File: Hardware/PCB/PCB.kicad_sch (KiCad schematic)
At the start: 0 parts

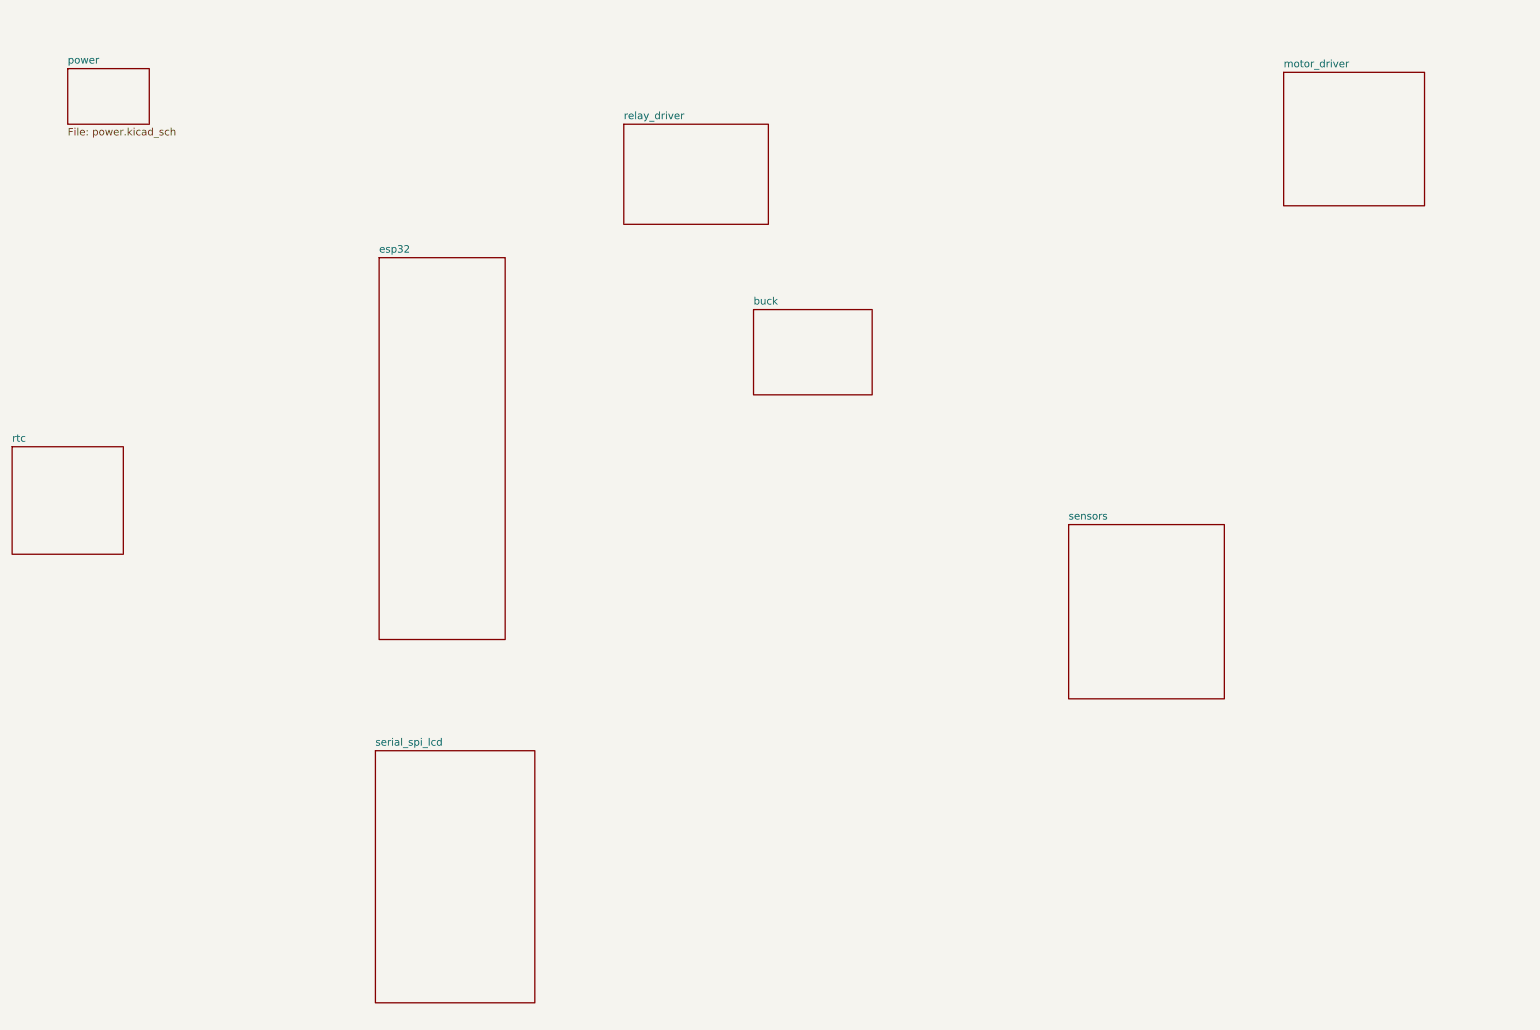
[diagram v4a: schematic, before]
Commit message: consolidated IO for LCD block, broke out hierarchial pins, need to start wiring everything up and then on to layout
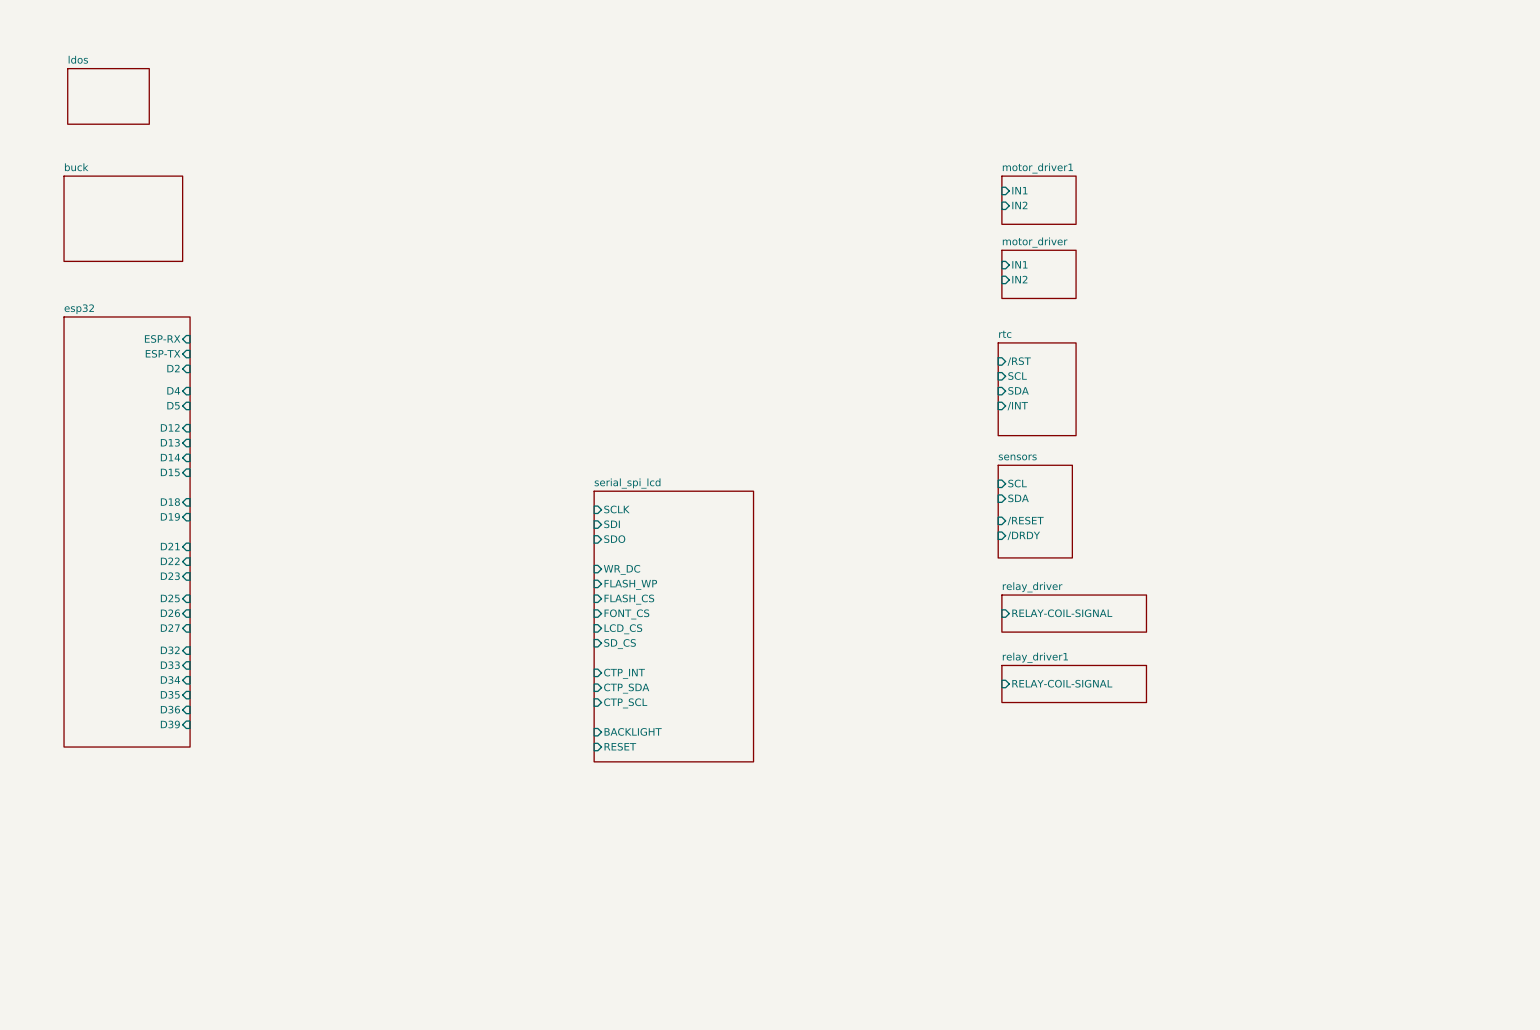
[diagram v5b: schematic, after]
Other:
- sheet power renamed ldos
- added sheet motor_driver1 (motor_driver.kicad_sch)
- added sheet relay_driver1 (relay_driver.kicad_sch)
- sheet esp32 ports: added D12, D13, D14, D15, D18, D19, D2, D21, D22, D23, D25, D26, D27, D32, D33, D34, D35, D36, D39, D4, D5, ESP-RX, ESP-TX; removed none
- sheet ldos: file power.kicad_sch -> ldos.kicad_sch
- sheet motor_driver ports: added IN1, IN2; removed none
- sheet relay_driver ports: added RELAY-COIL-SIGNAL; removed none
- sheet rtc ports: added SCL, SDA, /INT, /RST; removed none
- sheet sensors ports: added SCL, SDA, /DRDY, /RESET; removed none
- sheet serial_spi_lcd ports: added BACKLIGHT, CTP_INT, CTP_SCL, CTP_SDA, FLASH_CS, FLASH_WP, FONT_CS, LCD_CS, RESET, SCLK, SDI, SDO, SD_CS, WR_DC; removed none

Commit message: overall design is pretty much done, starting layout and routing now
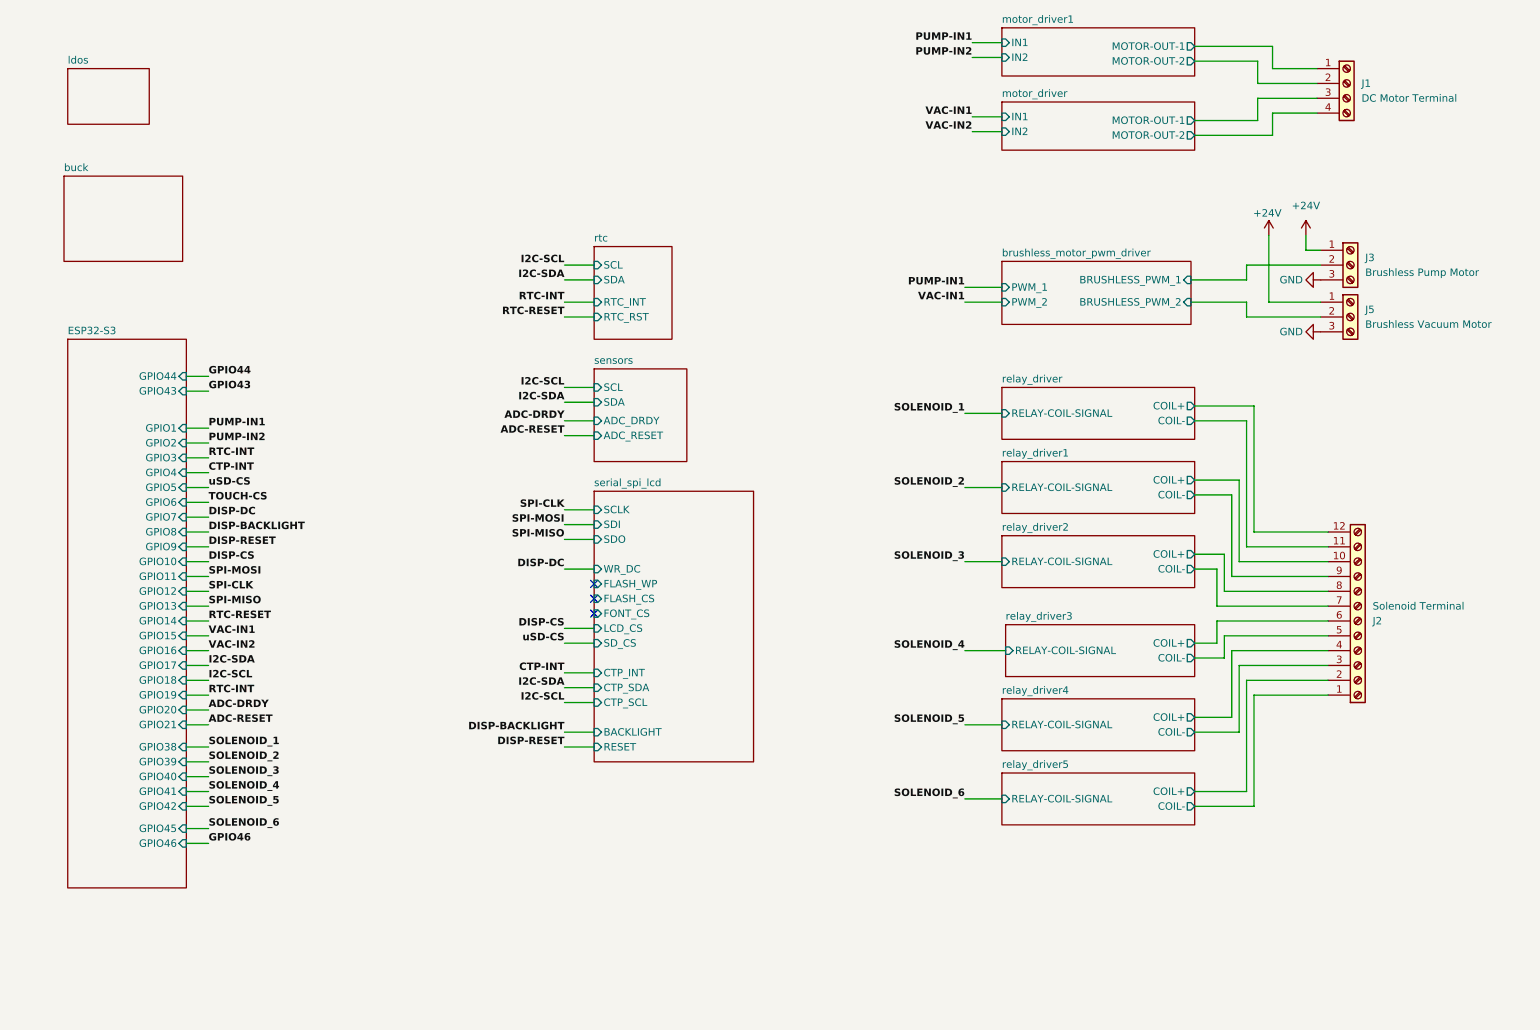
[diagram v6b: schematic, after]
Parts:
- added J1: DC Motor Terminal, Vendor_Footprints:TE_1985218, symbol Connector:Screw_Terminal_01x04
- added J2: Solenoid Terminal, Vendor_Footprints:PHX_16PIN_1985292, symbol Connector:Screw_Terminal_01x12
- added J3: Brushless Pump Motor, Vendor_Footprints:TE_1985205, symbol Connector:Screw_Terminal_01x03
- added J5: Brushless Vacuum Motor, Vendor_Footprints:TE_1985205, symbol Connector:Screw_Terminal_01x03
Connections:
- new net +24V: J3.1 (Pin_1), J5.1 (Pin_1)
- new net GND: J3.3 (Pin_3), J5.3 (Pin_3)
- new net brushless_motor_pwm_driver/BRUSHLESS_PWM_1: J3.2 (Pin_2)
- new net brushless_motor_pwm_driver/BRUSHLESS_PWM_2: J5.2 (Pin_2)
- new net motor_driver/MOTOR-OUT-1: J1.3 (Pin_3)
- new net motor_driver/MOTOR-OUT-2: J1.4 (Pin_4)
- new net motor_driver1/MOTOR-OUT-1: J1.1 (Pin_1)
- new net motor_driver1/MOTOR-OUT-2: J1.2 (Pin_2)
- new net relay_driver/COIL+: J2.12 (Pin_12)
- new net relay_driver/COIL-: J2.11 (Pin_11)
- new net relay_driver1/COIL+: J2.10 (Pin_10)
- new net relay_driver1/COIL-: J2.9 (Pin_9)
- new net relay_driver2/COIL+: J2.8 (Pin_8)
- new net relay_driver2/COIL-: J2.7 (Pin_7)
- new net relay_driver3/COIL+: J2.6 (Pin_6)
- new net relay_driver3/COIL-: J2.5 (Pin_5)
- new net relay_driver4/COIL+: J2.4 (Pin_4)
- new net relay_driver4/COIL-: J2.3 (Pin_3)
- new net relay_driver5/COIL+: J2.2 (Pin_2)
- new net relay_driver5/COIL-: J2.1 (Pin_1)
- no-connect marks 0 -> 3
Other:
- removed sheet esp32
- added sheet ESP32-S3 (esp32.kicad_sch)
- added sheet brushless_motor_pwm_driver (brushless_motor_pwm_driver.kicad_sch)
- added sheet relay_driver2 (relay_driver.kicad_sch)
- added sheet relay_driver3 (relay_driver.kicad_sch)
- added sheet relay_driver4 (relay_driver.kicad_sch)
- added sheet relay_driver5 (relay_driver.kicad_sch)
- sheet motor_driver ports: added MOTOR-OUT-1, MOTOR-OUT-2; removed none
- sheet motor_driver1 ports: added MOTOR-OUT-1, MOTOR-OUT-2; removed none
- sheet relay_driver ports: added COIL+, COIL-; removed none
- sheet relay_driver1 ports: added COIL+, COIL-; removed none
- sheet rtc ports: added RTC_INT, RTC_RST; removed /INT, /RST
- sheet sensors ports: added ADC_DRDY, ADC_RESET; removed /DRDY, /RESET

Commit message: pcb layout and routing pretty much done, checking DRC
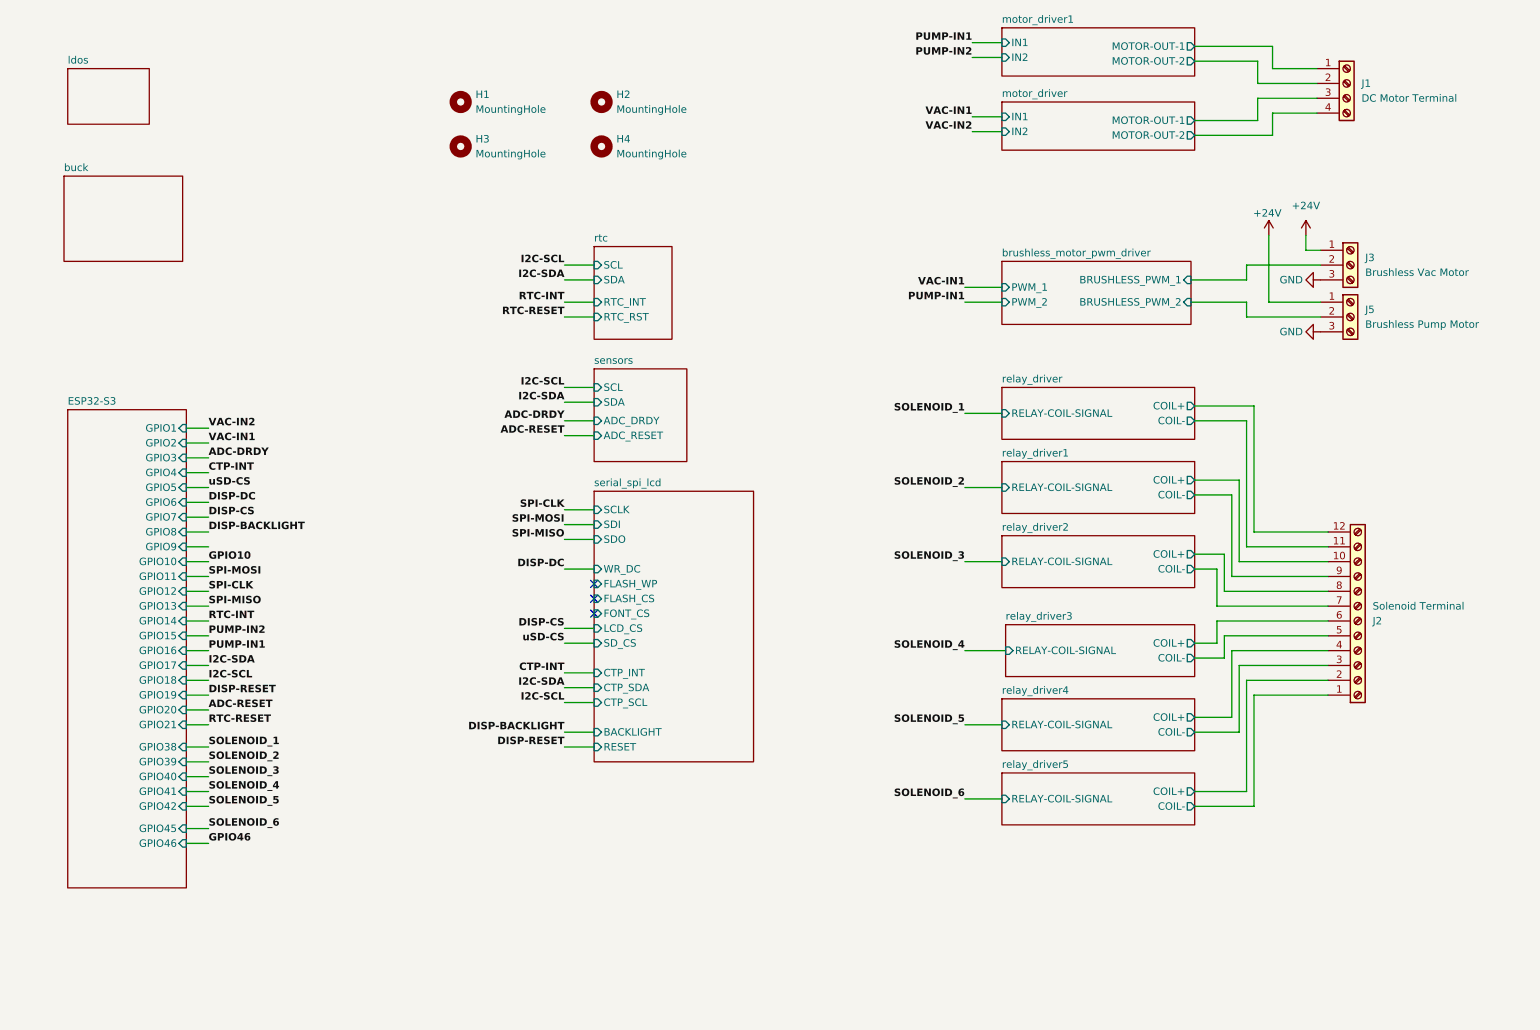
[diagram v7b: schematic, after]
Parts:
- added H1, H2, H3, H4: MountingHole, MountingHole:MountingHole_3.2mm_M3, symbol Mechanical:MountingHole
- J3: value Brushless Pump Motor -> Brushless Vac Motor
- J5: value Brushless Vacuum Motor -> Brushless Pump Motor
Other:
- sheet ESP32-S3 ports: added none; removed GPIO43, GPIO44

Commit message: kinda pricey, I should try to make a smaller version using LCSC parts for cheaper solution
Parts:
- J1: LCSC (none) -> C3820242
- J2: LCSC (none) -> C7435015
- J3, J5: LCSC (none) -> C3817619
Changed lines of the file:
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@@
+			)
+		)
+		(property "LCSC" ""
+			(at 129.54 30.48 0)
+			(effects
+				(font
+					(size 1.27 1.27)
+				)
 			)
 		)
@@
 			)
 		)
+		(property "LCSC" ""
+			(at 105.41 38.1 0)
+			(effects
+				(font
+					(size 1.27 1.27)
+				)
+			)
+		)
 		(instances
 			(project "PCB"
@@
 			)
 		)
+		(property "LCSC" "C3820242"
+			(at 257.175 27.305 0)
+			(effects
+				(font
+					(size 1.27 1.27)
+				)
+			)
+		)
 		(pin "4"
 		)
@@
 			)
 		)
+		(property "LCSC" ""
+			(at 105.41 30.48 0)
+			(effects
+				(font
+					(size 1.27 1.27)
+				)
+			)
+		)
 		(instances
 			(project ""
@@
 			)
 		)
+		(property "LCSC" "C3817619"
+			(at 257.81 67.31 0)
+			(effects
+				(font
+					(size 1.27 1.27)
+				)
+			)
+		)
 		(pin "3"
 		)
@@
 			)
 		)
+		(property "LCSC" "C3817619"
+			(at 257.81 58.42 0)
+			(effects
+				(font
+					(size 1.27 1.27)
+				)
+			)
+		)
 		(pin "3"
 		)
@@
 			)
 		)
+		(property "LCSC" ""
+			(at 129.54 38.1 0)
+			(effects
+				(font
+					(size 1.27 1.27)
+				)
+			)
+		)
 		(instances
 			(project "PCB"
@@
 			)
 		)
+		(property "LCSC" "C7435015"
+			(at 259.08 119.38 0)
+			(effects
+				(font
+					(size 1.27 1.27)
+				)
+			)
+		)
